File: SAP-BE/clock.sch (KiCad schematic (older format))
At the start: 22 parts, among them SW1 SW_SPDT, SW2 SW_Push, U30 NE555, U31 NE555, U32 74LS04, U33 74LS08, U34 74LS32, U6 NE555

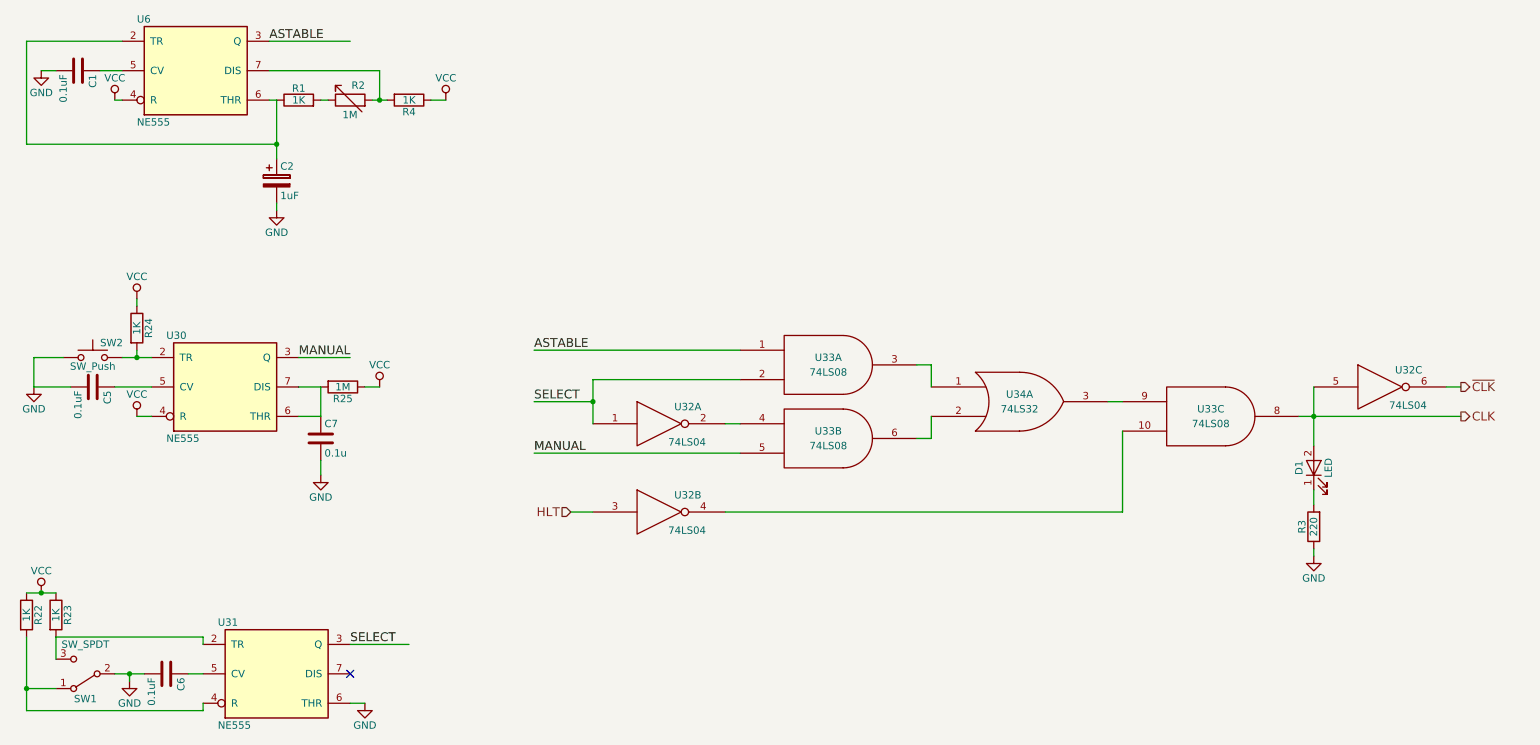
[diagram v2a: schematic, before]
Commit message: Microcode EPROM A7 used as bank select
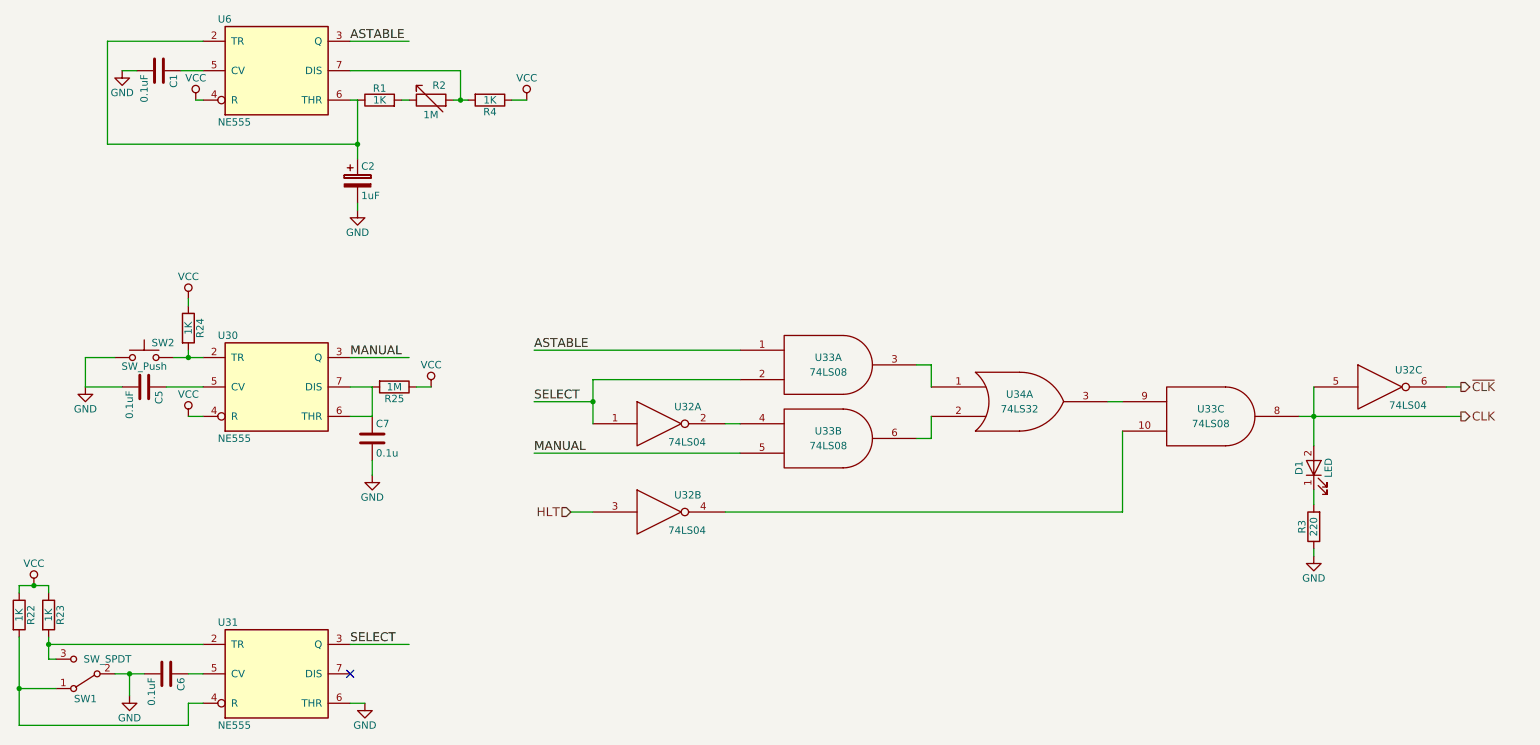
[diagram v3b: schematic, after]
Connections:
- wire segments 61 -> 64
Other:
- moved on the sheet: C1, C2, C5, C7, R1, R2, R22, R23, R24, R25, R4, SW2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
